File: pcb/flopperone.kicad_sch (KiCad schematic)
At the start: 0 parts

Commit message: minimum system
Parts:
- added C16, C17: 10uF, symbol Device:C
- added D1: 1N5819WS, Diode_SMD:D_SOD-323, symbol Diode:1N5819WS
- added J1: USB_C_Receptacle_USB2.0_14P, symbol Connector:USB_C_Receptacle_USB2.0_14P
- added R4, R5: 27R, symbol Device:R
- added U2: MCP1700x-330xxTT, Package_TO_SOT_SMD:SOT-23, symbol Regulator_Linear:MCP1700x-330xxTT
- added U3: USBLC6-2SC6, Package_TO_SOT_SMD:SOT-23-6, symbol Power_Protection:USBLC6-2SC6
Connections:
- new net: J1.A5 (CC1), R4.1
- new net: J1.A6 (D+), J1.B6 (D+), U3.3 (I/O2)
- new net: J1.A7 (D-), J1.B7 (D-), U3.1 (I/O1)
- new net: J1.B5 (CC2), R5.2
- new net +3V3: C17.1, U2.2 (VO)
- new net GND: C16.2, C17.2, J1.A1 (GND), J1.A12 (GND), J1.B1 (GND), J1.B12 (GND), J1.S1 (SHIELD), R4.2, R5.1, U2.1 (GND), U3.2 (GND)
- new net USB_DM: U3.6 (I/O1)
- new net USB_DP: U3.4 (I/O2)
- new net VBUS: D1.2 (A), J1.A4 (VBUS), J1.A9 (VBUS), J1.B4 (VBUS), J1.B9 (VBUS), U3.5 (VBUS)
- new net VSYS: C16.1, D1.1 (K), U2.3 (VI)
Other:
- added sheet rp2350 minimum system (rp2350.kicad_sch)
- note added: "Other Pages"
- note added: "Power (LDO)"
- note added: "USB-C"
- company: (none) -> Cybdo
- title: (none) -> FlopperOne

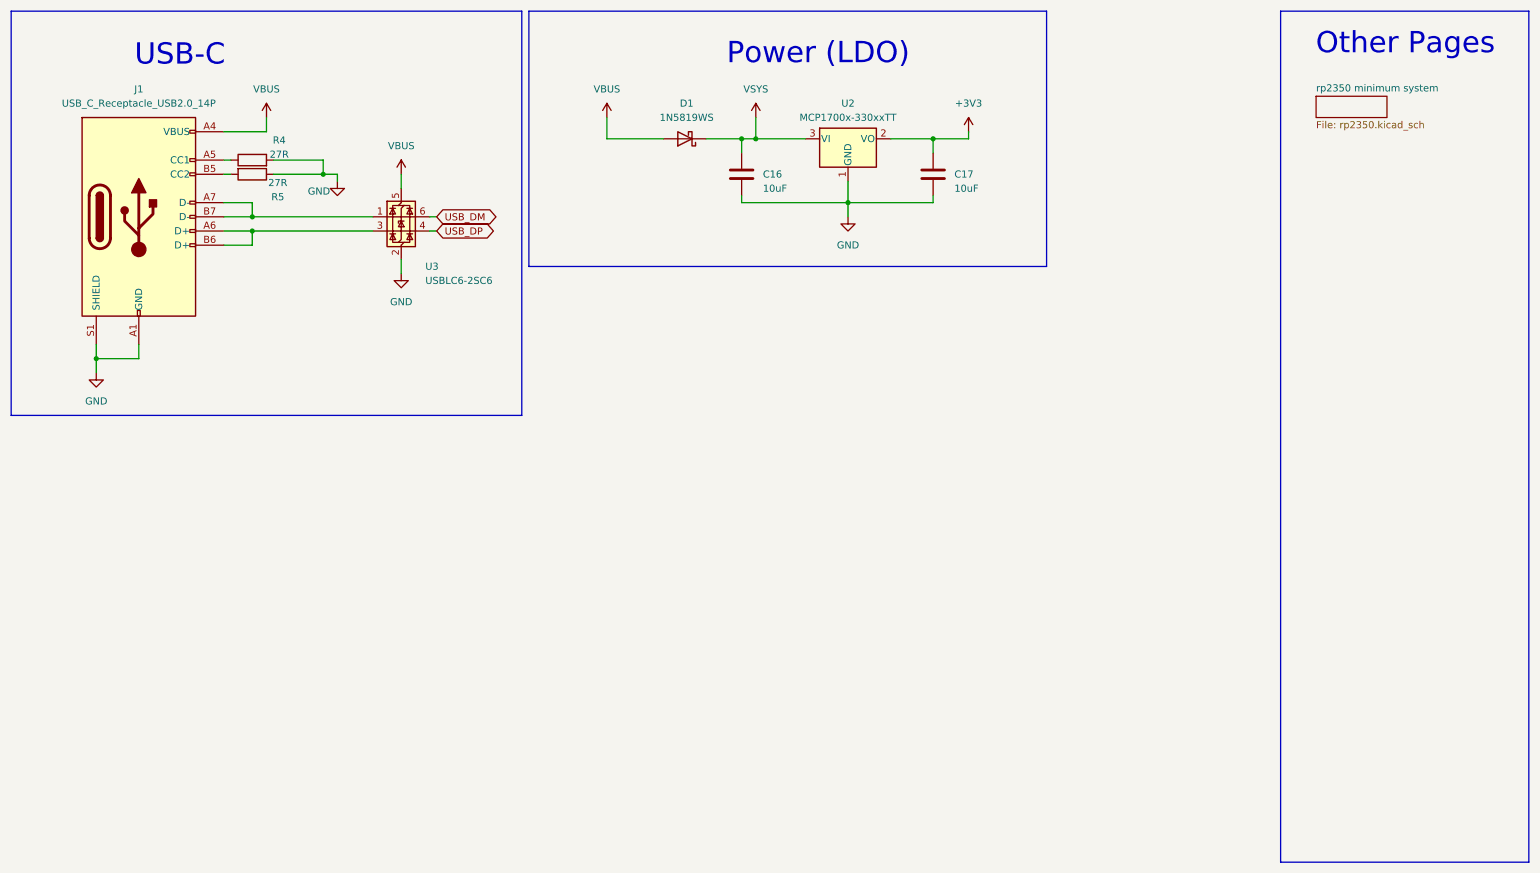
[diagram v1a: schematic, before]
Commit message: nfc and battery charge stuff
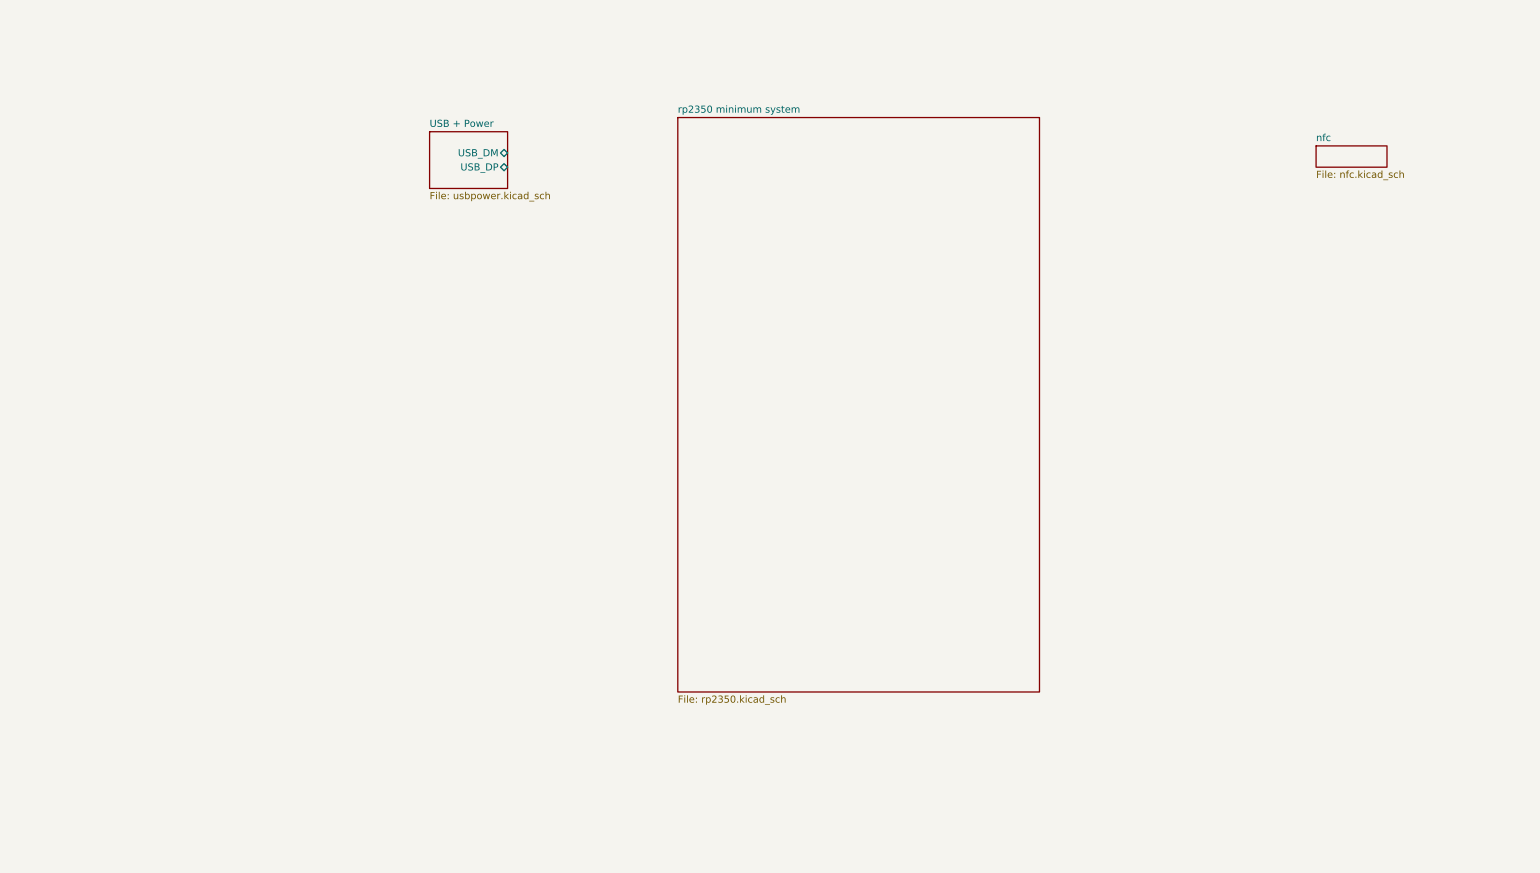
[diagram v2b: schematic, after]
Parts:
- removed C16, C17: 10uF, symbol Device:C
- removed D1: 1N5819WS, Diode_SMD:D_SOD-323, symbol Diode:1N5819WS
- removed J1: USB_C_Receptacle_USB2.0_14P, symbol Connector:USB_C_Receptacle_USB2.0_14P
- removed R4, R5: 27R, symbol Device:R
- removed U2: MCP1700x-330xxTT, Package_TO_SOT_SMD:SOT-23, symbol Regulator_Linear:MCP1700x-330xxTT
- removed U3: USBLC6-2SC6, Package_TO_SOT_SMD:SOT-23-6, symbol Power_Protection:USBLC6-2SC6
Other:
- added sheet USB + Power (usbpower.kicad_sch)
- added sheet nfc (nfc.kicad_sch)
- note removed: "Other Pages"
- note removed: "Power (LDO)"
- note removed: "USB-C"

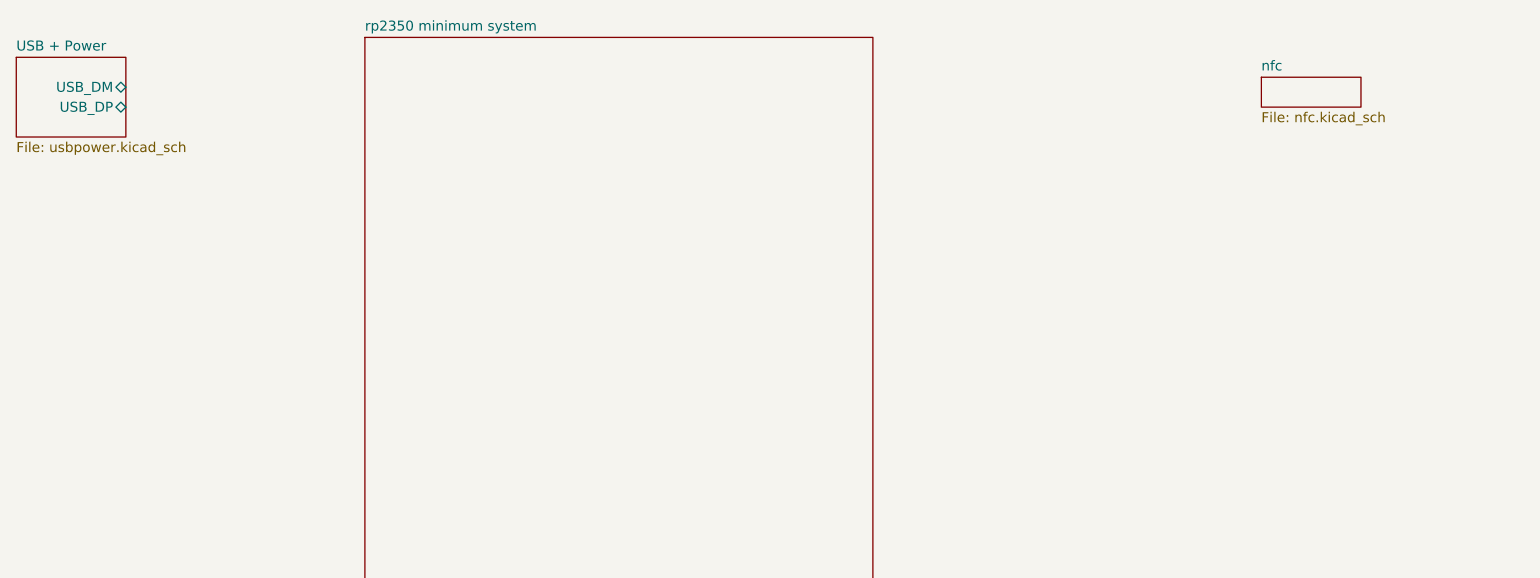
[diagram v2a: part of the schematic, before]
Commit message: nfc tuning, new charger IC
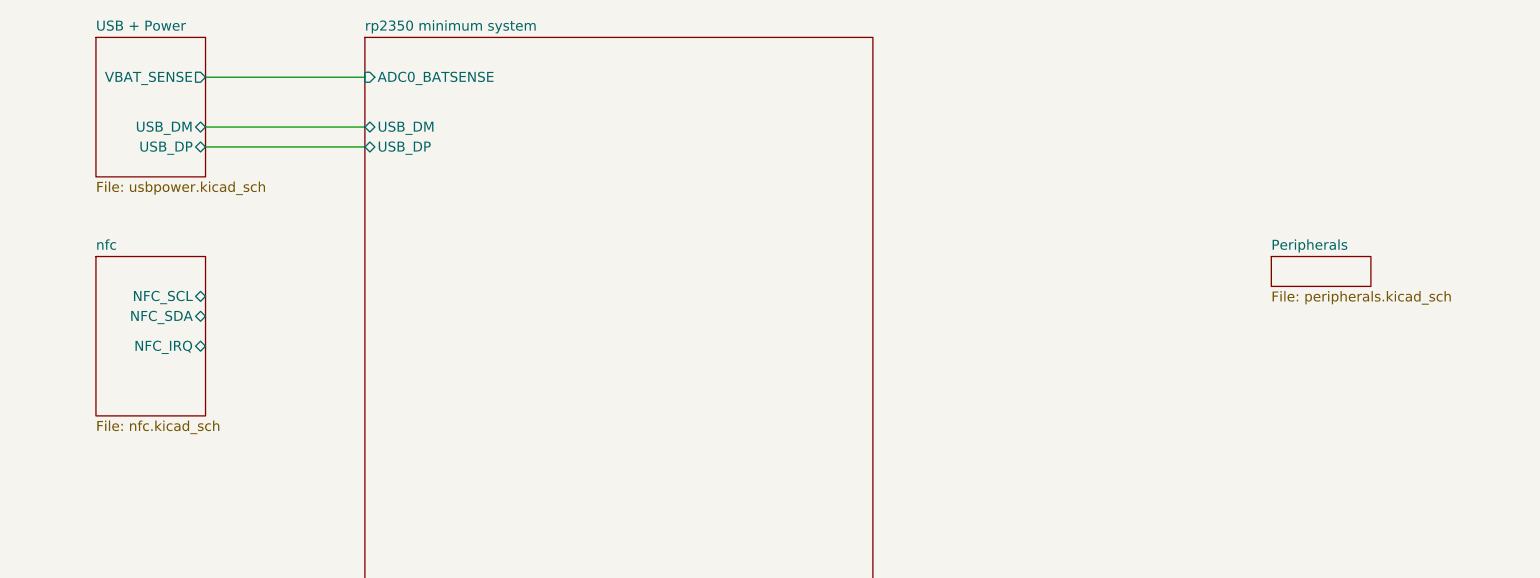
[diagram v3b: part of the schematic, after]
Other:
- added sheet Peripherals (peripherals.kicad_sch)
- sheet USB + Power ports: added VBAT_SENSE; removed none
- sheet nfc ports: added NFC_IRQ, NFC_SCL, NFC_SDA; removed none
- sheet rp2350 minimum system ports: added ADC0_BATSENSE, USB_DM, USB_DP; removed none
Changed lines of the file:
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@@
 		(company "Cybdo")
 	)
-	(sheet
-		(at 246.38 36.83)
-		(size 12.7 3.81)
+	(wire
+		(pts
+			(xy 111.76 43.18) (xy 132.08 43.18)
+		)
+		(stroke
+			(width 0)
+			(type default)
+		)
+	)
+	(wire
+		(pts
+			(xy 111.76 36.83) (xy 132.08 36.83)
+		)
+		(stroke
+			(width 0)
+			(type default)
+		)
+	)
+	(wire
+		(pts
+			(xy 111.76 45.72) (xy 132.08 45.72)
+		)
+		(stroke
+			(width 0)
+			(type default)
+		)
+	)
+	(sheet
+		(at 97.79 59.69)
+		(size 13.97 20.32)
 		(exclude_from_sim no)
 		(in_bom yes)
@@
 		)
 		(property "Sheetname" "nfc"
-			(at 246.38 36.1184 0)
+			(at 97.79 58.9784 0)
 			(effects
 				(font
@@
 		)
 		(property "Sheetfile" "nfc.kicad_sch"
-			(at 246.38 41.2246 0)
-			(effects
-				(font
-					(size 1.27 1.27)
-				)
-				(justify left top)
+			(at 97.79 80.5946 0)
+			(effects
+				(font
+					(size 1.27 1.27)
+				)
+				(justify left top)
+			)
+		)
+		(pin "NFC_IRQ" bidirectional
+			(at 111.76 71.12 0)
+			(effects
+				(font
+					(size 1.27 1.27)
+				)
+				(justify right)
+			)
+		)
+		(pin "NFC_SCL" bidirectional
+			(at 111.76 64.77 0)
+			(effects
+				(font
+					(size 1.27 1.27)
+				)
+				(justify right)
+			)
+		)
+		(pin "NFC_SDA" bidirectional
+			(at 111.76 67.31 0)
+			(effects
+				(font
+					(size 1.27 1.27)
+				)
+				(justify right)
 			)
 		)
@@
 			)
 		)
+		(pin "ADC0_BATSENSE" input
+			(at 132.08 36.83 180)
+			(effects
+				(font
+					(size 1.27 1.27)
+				)
+				(justify left)
+			)
+		)
+		(pin "USB_DM" bidirectional
+			(at 132.08 43.18 180)
+			(effects
+				(font
+					(size 1.27 1.27)
+				)
+				(justify left)
+			)
+		)
+		(pin "USB_DP" bidirectional
+			(at 132.08 45.72 180)
+			(effects
+				(font
+					(size 1.27 1.27)
+				)
+				(justify left)
+			)
+		)
 		(instances
 			(project "flopperone"
@@
 	)
 	(sheet
-		(at 87.63 34.29)
-		(size 13.97 10.16)
+		(at 97.79 31.75)
+		(size 13.97 17.78)
 		(exclude_from_sim no)
 		(in_bom yes)
@@
 		)
 		(property "Sheetname" "USB + Power"
-			(at 87.63 33.5784 0)
+			(at 97.79 31.0384 0)
 			(effects
 				(font
@@
 		)
 		(property "Sheetfile" "usbpower.kicad_sch"
-			(at 87.63 45.0346 0)
+			(at 97.79 50.1146 0)
 			(effects
 				(font
@@
 		)
 		(pin "USB_DM" bidirectional
-			(at 101.6 38.1 0)
+			(at 111.76 43.18 0)
 			(effects
 				(font
@@
 		)
 		(pin "USB_DP" bidirectional
-			(at 101.6 40.64 0)
+			(at 111.76 45.72 0)
+			(effects
+				(font
+					(size 1.27 1.27)
+				)
+				(justify right)
+			)
+		)
+		(pin "VBAT_SENSE" output
+			(at 111.76 36.83 0)
 			(effects
 				(font
@@
 				)
 			)
+		)
+	)
+	(sheet
+		(at 247.65 59.69)
+		(size 12.7 3.81)
+		(exclude_from_sim no)
+		(in_bom yes)
+		(on_board yes)
+		(dnp no)
+		(fields_autoplaced yes)
+		(stroke
+			(width 0.1524)
+			(type solid)
+		)
+		(fill
+			(color 0 0 0 0.0000)
+		)
+		(property "Sheetname" "Peripherals"
+			(at 247.65 58.9784 0)
+			(effects
+				(font
+					(size 1.27 1.27)
+				)
+				(justify left bottom)
+			)
+		)
+		(property "Sheetfile" "peripherals.kicad_sch"
+			(at 247.65 64.0846 0)
+			(effects
+				(font
+					(size 1.27 1.27)
+				)
+				(justify left top)
+			)
+		)
+		(instances
+			(project "flopperone"
+				(path "/21842aa8-f461-4adb-8a2d-bf0920423cff"
+					(page "5")
+				)
+			)
